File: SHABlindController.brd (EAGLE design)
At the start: 83.8 x 25.4 mm, 48 parts, among them IC1 ATMEGA1284P-TQFP, IC2 XBEE-1B2, IC3 MOC3042S, IC4 MOC3042S, SW1 RESET, T1 MOC3042M, T2 MOC3042M, Y1 RESONATORSMD

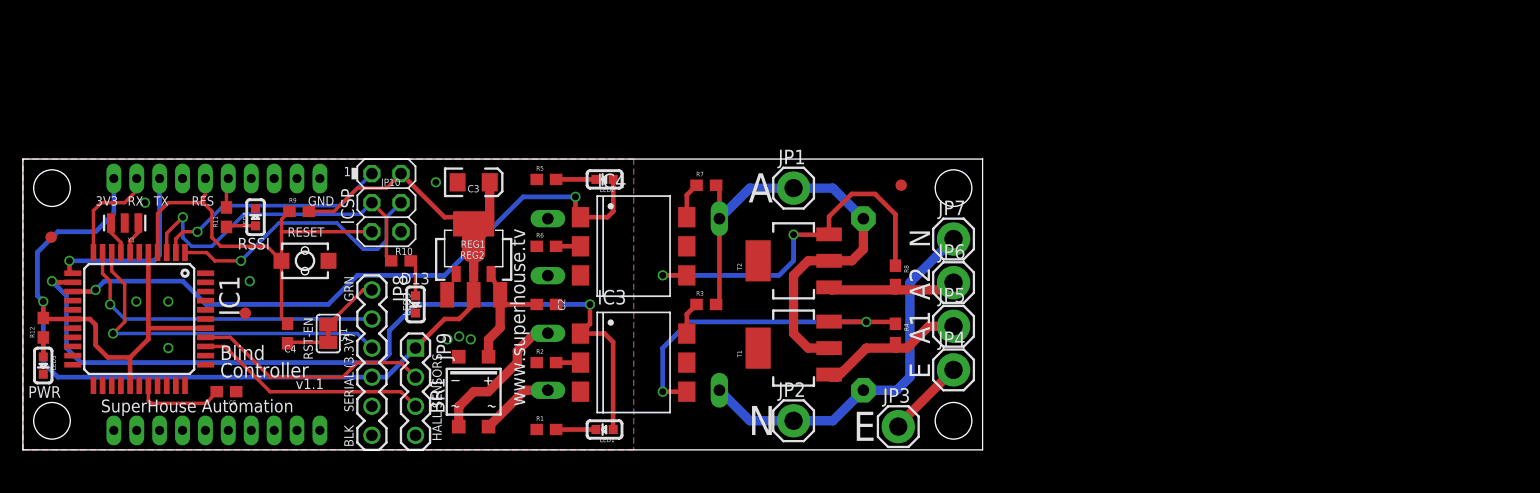
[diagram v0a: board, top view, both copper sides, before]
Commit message: Reshaped board to fit blind mounts
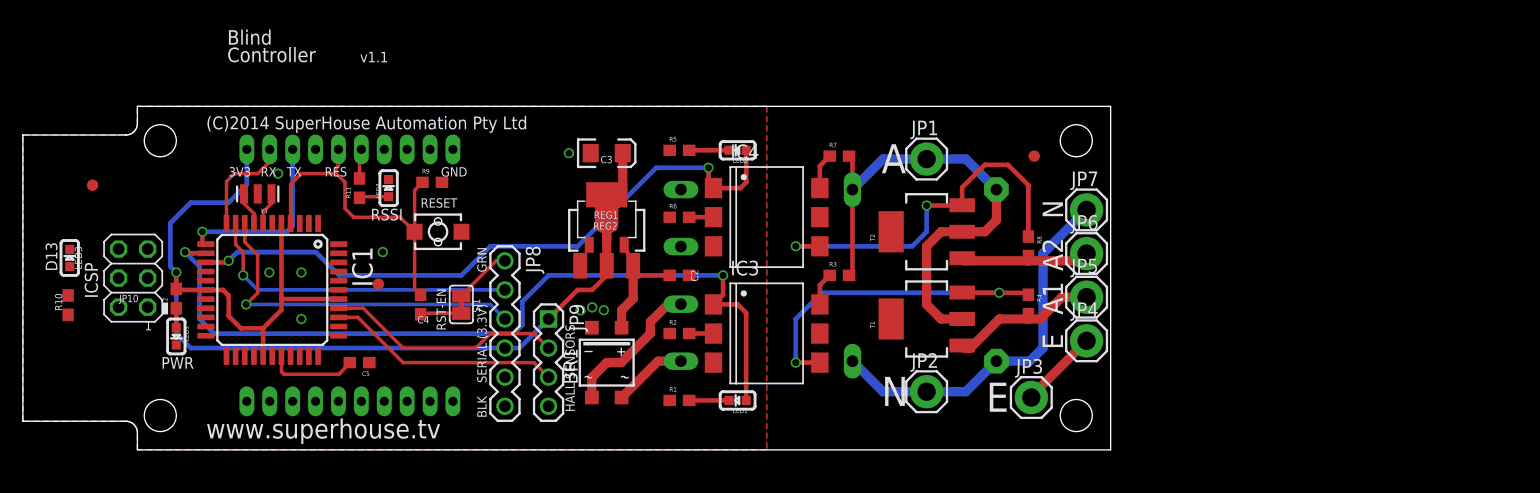
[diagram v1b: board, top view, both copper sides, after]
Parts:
- moved LED3 30.5 mm to (4.09, 16.8), turned to 0 degrees
- moved R10 29.3 mm to (3.95, 12.6), turned to 270 degrees
- moved JP10 23.1 mm to (9.63, 15.0), turned to 90 degrees
- moved BR1 11.9 mm to (51.0, 7.62)
- moved C2 11.9 mm to (57.3, 15.2)
- moved C3 11.9 mm to (51.0, 25.9)
- moved FID1 11.9 mm to (88.3, 25.7)
- moved JP1 11.9 mm to (78.9, 25.4)
- moved JP2 11.9 mm to (78.9, 5.08)
- moved JP3 11.9 mm to (88.1, 4.57)
- moved JP4 11.9 mm to (92.9, 9.53)
- moved JP5 11.9 mm to (92.9, 13.3)
- moved JP6 11.9 mm to (92.9, 17.1)
- moved JP7 11.9 mm to (92.9, 21.0)
- moved LED1 11.9 mm to (62.4, 4.32)
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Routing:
- net D13_SCK: track 29.6 -> 0.00 mm, vias 1 -> 0
- net D11_MOSI: track 24.3 -> 0.00 mm, vias 1 -> 0
- net D12_MISO: track 20.7 -> 0.00 mm, vias 1 -> 0
- net VCC: track 120.1 -> 103.3 mm
- net RESET: track 38.5 -> 30.6 mm
- net N$1: track 3.23 -> 0.00 mm
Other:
- board size 83.8 x 25.4 mm -> 95 x 30 mm
- board text added: "(C)2014 SuperHouse Automation Pty Ltd"
- board text removed: "SuperHouse Automation"

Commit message: Replaced MCU and XBee with Spark Core
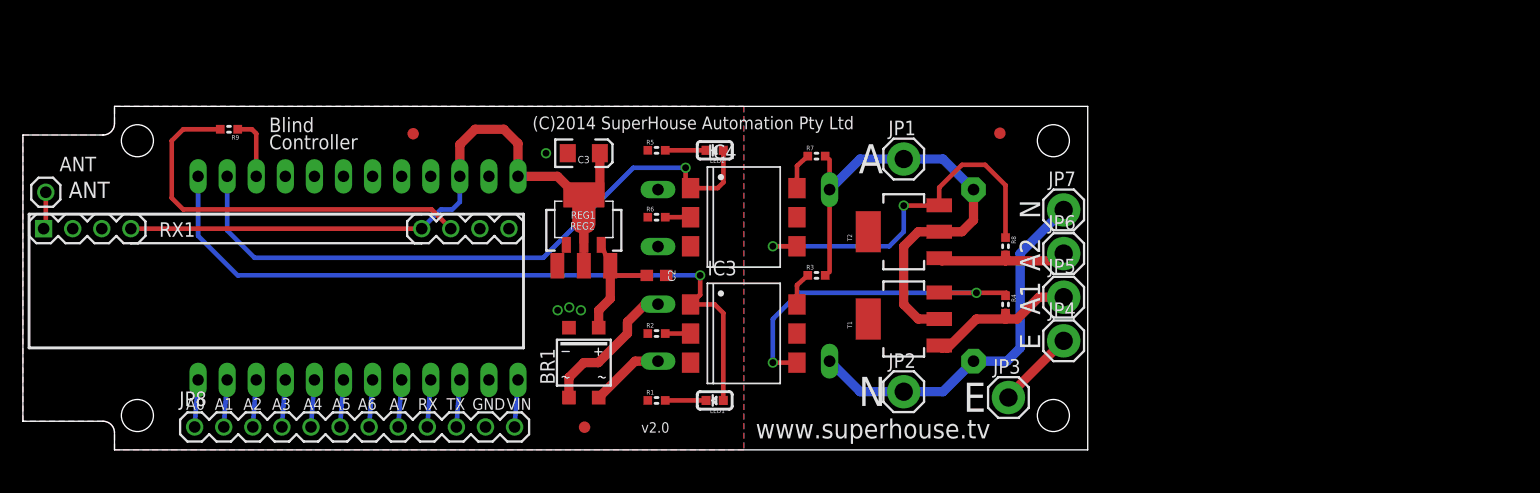
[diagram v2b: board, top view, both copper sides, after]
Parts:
- removed C4, C5: 100nF 0603, freetronics:0603
- removed IC2: XBEE-1B2, xbee:XBEE-SILK
- removed JP10: ICSP:MAIN, pinhead:2X03
- removed JP9: (no value), freetronics-original:1X04
- removed LED3, LED5: D13/RED, freetronics:LED-0603
- removed LED4: RSSI/RED, freetronics:LED-0603
- removed R10, R12: 220R 0603, freetronics:0603
- removed R11: 150R 0603, freetronics:0603
- removed SJ1: RESET-EN, freetronics-jon:SJC
- removed SW1: RESET, freetronics-master-v1:TACTILE_SWITCH_SMD_2PIN_TINY
- removed Y1: RESONATORSMD, SparkFun:RESONATOR-SMD
- added ANT: M01PTH, freetronics:1X01
- added RX1: RXB1SIL, PracticalArduino:RX-B1
- C2: device freetronics:0603 -> freetronics:0603@1
- IC1: value ATMEGA1284P-TQFP -> SPARKCORE; device freetronics-jon:TQFP44 -> freetronics-jon:SPARKCORE
- JP8: value (none) -> M12PTH; device freetronics-master-v1.1:1X06 -> freetronics-original:1X12
- R9: value 10K 0603 -> 1K
- moved JP8 30.7 mm to (15.0, 2.00), turned to 0 degrees
- moved FID2 28.4 mm to (34.1, 27.6)
- moved FID3 21.9 mm to (49.1, 1.98)
- moved R9 18.3 mm to (18.0, 28.0), turned to 180 degrees
- moved IC1 6.30 mm to (28.0, 15.0), flipped to the bottom
- moved FID1 3.61 mm to (85.3, 27.7)
- moved BR1 2.00 mm to (49.0, 7.62)
- moved C1 2.00 mm to (83.0, 15.2)
- moved C2 2.00 mm to (55.3, 15.2)
- moved C3 2.00 mm to (49.0, 25.9)
- moved JP1 2.00 mm to (76.9, 25.4)
- moved JP2 2.00 mm to (76.9, 5.08)
- moved JP3 2.00 mm to (86.1, 4.57)
- moved JP4 2.00 mm to (90.9, 9.53)
- moved JP5 2.00 mm to (90.9, 13.3)
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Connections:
- removed net D0_RX: IC1.9, JP8.3
- removed net D10: IC1.44
- removed net D11_MOSI: IC1.1, JP10.4
- removed net D12_MISO: IC1.2, JP10.1
- removed net D13_SCK: IC1.3, JP10.3, R10.2
- removed net D1_TX: IC1.10, JP8.2
- removed net D2_RX1: IC1.11, IC2.2
- removed net D3_TX1: IC1.12, IC2.3
- removed net D4: IC1.13, IC3.1, LED1.A
- removed net D5: IC1.14, IC4.1, LED2.A
- removed net D6: IC1.15
- removed net D7: IC1.16
- removed net D8: IC1.42
- removed net D9: IC1.43
- removed net DTR: JP8.1, SJ1.1
- removed net N$11: C5.2, IC1.29
- removed net N$19: LED5.A, R12.1
- removed net N$23: IC2.6, R11.2
- removed net N$24: LED4.A, R11.1
- removed net N$8: IC1.7, Y1.1
- removed net N$9: IC1.8, Y1.3
- removed net RESET: C4.2, IC1.4, IC2.5, JP10.5, R9.1, SW1.2
- new net D0: IC1.P$1, IC3.1, LED1.A
- new net D1: IC1.P$2, IC4.1, LED2.A
- new net N$135: R9.2, RX1.23
- new net RX: IC1.P$16, JP8.9
- new net TX: IC1.P$15, JP8.10
- new net VIN: IC1.P$13, JP8.12
- net A0: now also IC1.P$24, JP8.1; no longer IC1.37, JP9.2
- net A1: now also IC1.P$23, JP8.2; no longer IC1.36, JP9.3
- net A2: now also IC1.P$22, JP8.3; no longer IC1.35
- net A3: now also IC1.P$21, JP8.4; no longer IC1.34
- net A4: now also IC1.P$20, JP8.5; no longer IC1.33
- net A5: now also IC1.P$19, JP8.6; no longer IC1.32
- net A6: now also IC1.P$18, JP8.7; no longer IC1.31
- net A7: now also IC1.P$17, JP8.8; no longer IC1.30
- net GND: now also IC1.P$14, IC1.P$9, JP8.11, RX1.10, RX1.11, RX1.25; no longer C5.1, IC1.18, IC1.28, IC1.39, IC1.6, IC2.10, JP10.6, JP8.5, JP8.6, JP9.4, LED3.C, LED4.C, LED5.C, SW1.1, Y1.2
- net N$1: now also ANT.1, RX1.9; no longer LED3.A, R10.1
- net N$3: now also IC1.P$3, R9.1; no longer C4.1, SJ1.2
- net VCC: now also IC1.P$10, IC1.P$12, RX1.12, RX1.22; no longer IC1.17, IC1.27, IC1.38, IC1.5, IC2.1, JP10.2, JP8.4, JP9.1, R12.2, R9.2
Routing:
- net D4: track 71.4 -> 0.00 mm, vias 2 -> 0
- net D0: track 0.00 -> 64.2 mm, vias 0 -> 1
- net D1: track 0.00 -> 56.8 mm, vias 0 -> 1
- net D5: track 56.8 -> 0.00 mm, vias 2 -> 0
- net VCC: track 103.3 -> 62.2 mm, vias 1 -> 0
- net N$135: track 0.00 -> 35.1 mm
- net D0_RX: track 31.1 -> 0.00 mm, vias 1 -> 0
- net RESET: track 30.6 -> 0.00 mm
- net D1_TX: track 28.2 -> 0.00 mm, vias 1 -> 0
- net A0: track 20.8 -> 4.12 mm
- net D3_TX1: track 16.5 -> 0.00 mm, vias 1 -> 0
- net A1: track 20.5 -> 4.12 mm
- net D2_RX1: track 9.23 -> 0.00 mm
- net N$11: track 7.86 -> 0.00 mm
- net DTR: track 5.07 -> 0.00 mm
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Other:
- board size 95 x 30 mm -> 93 x 30 mm
- board text added: "A0"
- board text added: "A3"
- board text added: "A4"
- board text added: "A5"
- board text added: "A6"
- board text added: "A7"
- board text added: "ANT"
- board text added: "VIN"
- board text added: "v2.0"
- board text removed: "1"
- board text removed: "3V3"
- board text removed: "BLK"
- board text removed: "D13"
- board text removed: "GRN"
- board text removed: "HALL SENSORS"
- board text removed: "ICSP"
- board text removed: "K"
- board text removed: "PWR"
- board text removed: "RES"
- board text removed: "RESET"
- board text removed: "RSSI"
- board text removed: "RST-EN"
- board text removed: "SERIAL (3.3V)"
- board text removed: "v1.1"

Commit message: Improved routing for v2.0 release
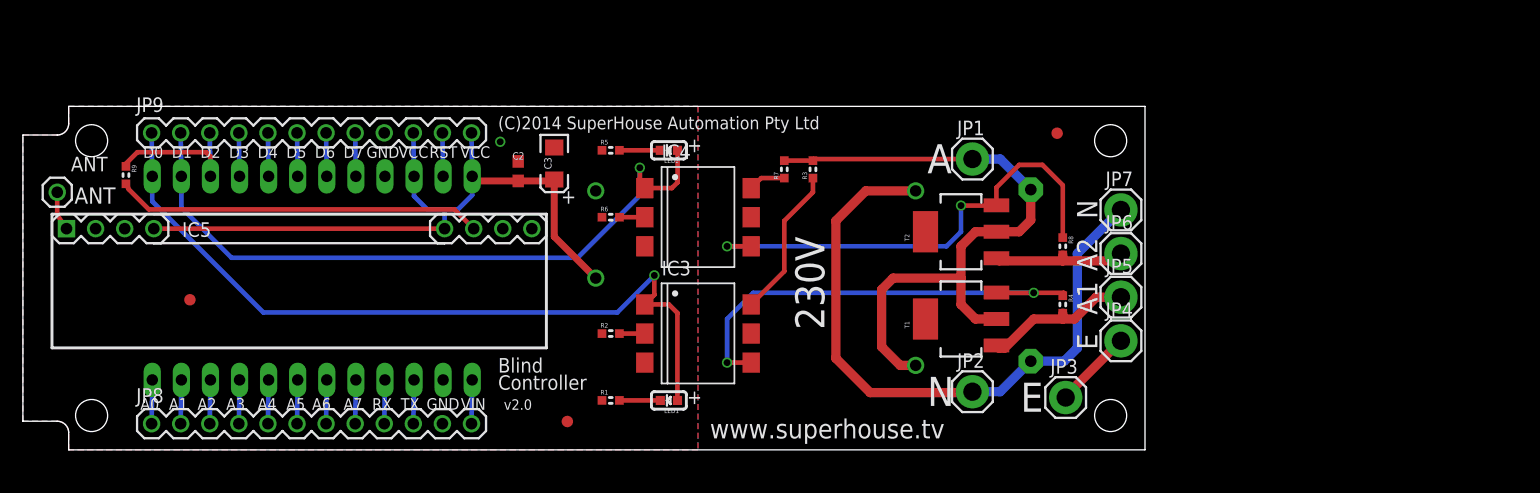
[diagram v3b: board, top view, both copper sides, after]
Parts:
- removed BR1: MB1S, rectifier:SOIC-4
- removed REG1: LD1117-SOT89, freetronics:SOT89
- removed REG2: LD1117-SOT223, freetronics:SOT223
- removed RX1: RXB1SIL, PracticalArduino:RX-B1
- removed TR1: (no value), freetronics-jon:EE20-2
- added IC2: RAC02-3.3SC, freetronics-jon:RAC0X-SC
- added IC5: RXB1SIL, PracticalArduino:RX-B1
- added JP9: M12PTH, freetronics-original:1X12
- C1: value (none) -> 0.33uF 275V
- moved FID2 24.3 mm to (14.6, 13.1)
- moved C2 15.1 mm to (43.3, 24.3), turned to 90 degrees
- moved R9 9.85 mm to (9.00, 24.0), turned to 270 degrees
- moved R3 9.27 mm to (69.0, 24.5), turned to 90 degrees
- moved JP1 6.00 mm to (82.9, 25.4)
- moved JP2 6.00 mm to (82.9, 5.08)
- moved C1 5.00 mm to (88.0, 15.2)
- moved FID1 5.00 mm to (90.3, 27.7)
- moved JP3 5.00 mm to (91.1, 4.57)
- moved JP4 5.00 mm to (95.9, 9.53)
- moved JP5 5.00 mm to (95.9, 13.3)
- moved JP6 5.00 mm to (95.9, 17.1)
- moved JP7 5.00 mm to (95.9, 21.0)
- moved R4 5.00 mm to (90.8, 12.7)
- moved R8 5.00 mm to (90.8, 17.8)
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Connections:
- removed net N$3: IC1.P$3, R9.1
- removed net N$5: BR1.+, C2.1, REG1.3, REG2.3
- removed net N$6: BR1.~1, TR1.6
- removed net N$7: BR1.~2, TR1.5
- new net D2: IC1.P$3, JP9.3, R9.1
- new net D3: IC1.P$4, JP9.4
- new net D4: IC1.P$5, JP9.5
- new net D5: IC1.P$6, JP9.6
- new net D6: IC1.P$7, JP9.7
- new net D7: IC1.P$8, JP9.8
- new net RST: IC1.P$11, JP9.11
- net ACTIVE: now also IC2.2; no longer TR1.1
- net D0: now also JP9.1
- net D1: now also JP9.2
- net GND: now also IC2.3, IC5.10, IC5.11, IC5.25, JP9.9; no longer BR1.-, REG1.1, REG2.1, RX1.10, RX1.11, RX1.25
- net N$1: now also IC5.9; no longer RX1.9
- net N$135: now also IC5.23; no longer RX1.23
- net NEUTRAL: now also IC2.1; no longer TR1.4
- net VCC: now also C2.1, IC2.4, IC5.12, IC5.22, JP9.10, JP9.12; no longer REG1.2, REG1.4, REG2.2, REG2.4, RX1.12, RX1.22
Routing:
- net NEUTRAL: track 33.0 -> 57.6 mm
- net D2: track 0.00 -> 13.7 mm
- net ACTIVE: track 44.0 -> 57.2 mm
- net N$6: track 12.8 -> 0.00 mm
- net N$5: track 11.0 -> 0.00 mm
- net N$13: track 2.96 -> 13.3 mm
- net N$16: track 32.9 -> 41.9 mm
- net N$12: track 30.9 -> 39.9 mm
- net N$7: track 6.49 -> 0.00 mm
- net N$3: track 5.51 -> 0.00 mm
- net D0: track 64.2 -> 68.9 mm
- net D1: track 56.8 -> 60.9 mm
- net RST: track 0.00 -> 3.80 mm
- net D7: track 0.00 -> 3.80 mm
- net D6: track 0.00 -> 3.80 mm
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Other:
- board size 93 x 30 mm -> 98 x 30 mm
- board text added: "+"
- board text added: "230V"
- board text added: "D0"
- board text added: "D1"
- board text added: "D2"
- board text added: "D3"
- board text added: "D4"
- board text added: "D5"
- board text added: "D6"
- board text added: "D7"
- board text added: "RST"
- board text added: "VCC"
